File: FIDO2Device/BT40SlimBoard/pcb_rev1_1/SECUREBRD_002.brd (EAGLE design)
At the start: 30 x 30 mm, 31 parts, among them CN1 2137160001, CN2 IF_5PIN_H, CN3 IF_2PIN_SOL, SW1 SKRPACE010, SW2 SKRPACE010, SW3 SKTADAE010, U1 BT40, U2 ADP122ACPZ-3.3-R7

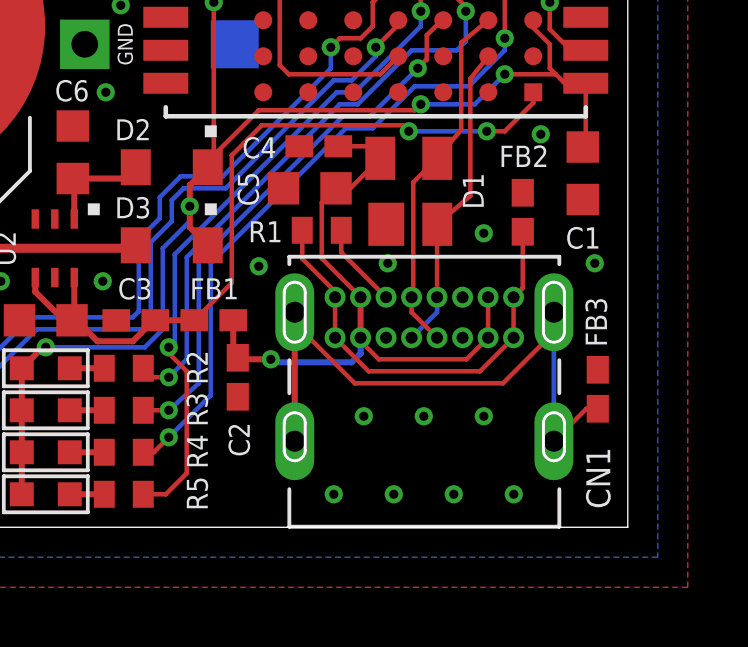
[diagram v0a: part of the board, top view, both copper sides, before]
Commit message: 回路図を更新
・USB-Cプラグ部品を`USB4105-GF-A`に更新
（前回試作失敗の原因となった部品`2137160001`から差し替え）
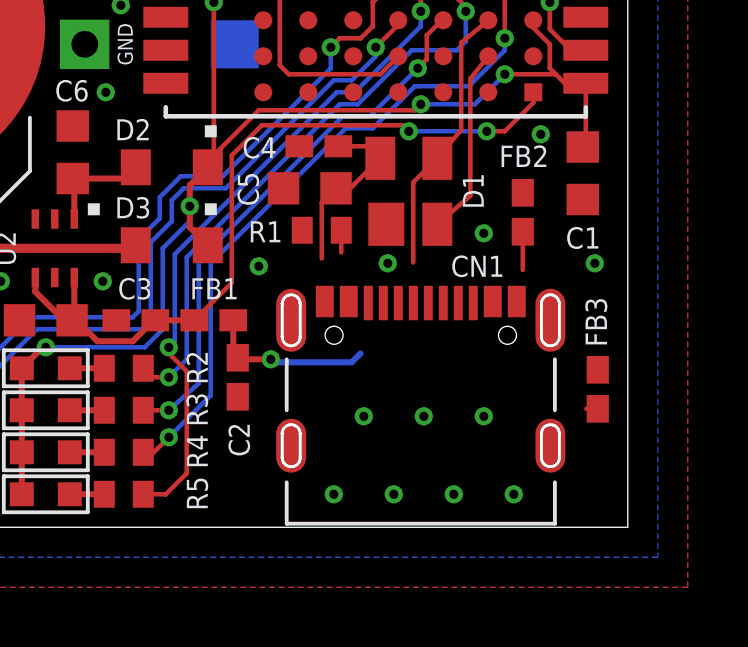
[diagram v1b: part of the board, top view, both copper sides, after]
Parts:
- CN1: value 2137160001 -> USB4105-GF-A; device Connectors:2137160001 -> Connectors:USB4105-GF-A
- moved CN1 0.29 mm to (23.1, 6.90)
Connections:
- net USB_GND: no longer CN1.A12, CN1.B12
- net VBUS: no longer CN1.A9, CN1.B9
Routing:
- net FG: track 21.7 -> 0.38 mm
- net USB_GND: track 14.6 -> 1.27 mm
- net VBUS: track 21.7 -> 11.6 mm
- net D_N: track 10.5 -> 6.32 mm
- net D_P: track 12.0 -> 9.12 mm
- net N$2: track 2.85 -> 0.74 mm
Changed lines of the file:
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@@
 <attribute name="VALUE" x="6.29" y="6.87" size="0.7" layer="27" rot="R270"/>
-</element>
-<element name="CN1" library="Connectors" package="2137160001" value="2137160001" x="23.2178" y="7.1688" smashed="yes">
-<attribute name="NAME" x="28.6178" y="2.6688" size="0.8" layer="25" rot="R270"/>
-<attribute name="VALUE" x="23.5178" y="9.3688" size="0.8" layer="27"/>
 </element>
 <element name="R1" library="Parts" package="R0402" value="5.1k" x="19.8" y="9.9" smashed="yes">
@@
 </element>
 <element name="CN3" library="Connectors" package="SOLPAD_2PIN" value="IF_2PIN_SOL" x="16.9" y="16.1" rot="MR90"/>
+<element name="CN1" library="Connectors" package="USB4105-GF-A" value="USB4105-GF-A" x="23.1" y="6.9" smashed="yes">
+<attribute name="NAME" x="24.1" y="8.35" size="0.7" layer="25"/>
+<attribute name="VALUE" x="23.4" y="8.5" size="0.8" layer="27"/>
+</element>
 </elements>
 <signals>
@@
 <contactref element="C5" pad="1"/>
 <contactref element="D1" pad="4"/>
-<contactref element="CN1" pad="A4"/>
-<contactref element="CN1" pad="B9"/>
-<contactref element="CN1" pad="A9"/>
-<contactref element="CN1" pad="B4"/>
-<wire x1="25.3428" y1="6.3188" x2="25.3428" y2="7.6688" width="0.1524" layer="1"/>
-<wire x1="21.0928" y1="7.6688" x2="21.0928" y2="6.3188" width="0.2032" layer="1"/>
-<wire x1="21.0928" y1="6.3188" x2="21.0928" y2="6.2072" width="0.1524" layer="1"/>
-<wire x1="21.0928" y1="6.2072" x2="21.7" y2="5.6" width="0.1524" layer="1"/>
-<wire x1="25.3428" y1="6.3188" x2="24.624" y2="5.6" width="0.1524" layer="1"/>
-<wire x1="24.624" y1="5.6" x2="21.7" y2="5.6" width="0.1524" layer="1"/>
-<wire x1="21.0928" y1="7.6688" x2="19.8" y2="8.9616" width="0.1524" layer="1"/>
 <wire x1="19.8" y1="8.9616" x2="19.8" y2="10.825" width="0.1524" layer="1"/>
 <wire x1="20.275" y1="11.3" x2="19.8" y2="10.825" width="0.1524" layer="1"/>
 <via x="18.1" y="5.6" extent="1-16" drill="0.3048"/>
-<wire x1="21.0928" y1="6.2072" x2="21.0928" y2="6.3188" width="0.1524" layer="16"/>
 <wire x1="16.85" y1="6.9" x2="16.85" y2="5.8" width="0.2032" layer="1"/>
 <wire x1="16.85" y1="5.8" x2="17" y2="5.65" width="0.2032" layer="1"/>
@@
 <wire x1="18.2" y1="5.5" x2="20.8" y2="5.5" width="0.2032" layer="16"/>
 <wire x1="20.8" y1="5.5" x2="21.0928" y2="5.7928" width="0.2032" layer="16"/>
-<wire x1="21.0928" y1="6.3188" x2="21.0928" y2="5.7928" width="0.2032" layer="16"/>
 <wire x1="20.275" y1="11.3" x2="20.75" y2="11.3" width="0.1524" layer="1"/>
 <wire x1="20.75" y1="11.3" x2="21.75" y2="12.3" width="0.1524" layer="1"/>
@@
 <wire x1="17.05" y1="5.6" x2="18.1" y2="5.6" width="0.2032" layer="1"/>
 <wire x1="18.2" y1="5.5" x2="18.1" y2="5.6" width="0.2032" layer="16"/>
+<contactref element="CN1" pad="A4"/>
+<contactref element="CN1" pad="B4"/>
+<wire x1="21.0928" y1="5.7928" x2="25.5" y2="7.525" width="0" layer="19" extent="1-16"/>
+<wire x1="20.7" y1="7.525" x2="21.0928" y2="5.7928" width="0" layer="19" extent="1-16"/>
+<wire x1="19.8" y1="8.9616" x2="20.7" y2="7.525" width="0" layer="19" extent="1-1"/>
 </signal>
 <signal name="USB_GND">
 <contactref element="FB2" pad="1"/>
-<contactref element="R1" pad="1"/>
-<contactref element="CN1" pad="A12"/>
+<wire x1="26.5" y1="9.85" x2="26.5" y2="8.576" width="0.1524" layer="1"/>
 <contactref element="CN1" pad="B1"/>
 <contactref element="CN1" pad="A1"/>
-<contactref element="CN1" pad="B12"/>
-<wire x1="26.5" y1="9.85" x2="26.5" y2="7.976" width="0.1524" layer="1"/>
-<wire x1="26.5" y1="7.976" x2="26.1928" y2="7.6688" width="0.1524" layer="1"/>
-<wire x1="20.2428" y1="6.3188" x2="20.2428" y2="7.6688" width="0.1524" layer="1"/>
-<wire x1="26.1928" y1="6.3188" x2="25.074" y2="5.2" width="0.1524" layer="1"/>
-<wire x1="20.2428" y1="6.3188" x2="21.3616" y2="5.2" width="0.1524" layer="1"/>
-<wire x1="26.1928" y1="6.3188" x2="26.1928" y2="7.6688" width="0.1524" layer="1"/>
-<wire x1="25.074" y1="5.2" x2="21.3616" y2="5.2" width="0.1524" layer="1"/>
-<wire x1="20.2428" y1="7.6688" x2="20.2428" y2="7.8572" width="0.1524" layer="1"/>
-<wire x1="20.2428" y1="7.8572" x2="19.15" y2="8.95" width="0.1524" layer="1"/>
-<wire x1="19.15" y1="9.9" x2="19.15" y2="8.95" width="0.1524" layer="1"/>
+<contactref element="R1" pad="1"/>
+<wire x1="26.3" y1="7.525" x2="26.5" y2="8.576" width="0" layer="19" extent="1-1"/>
+<wire x1="19.9" y1="7.525" x2="26.3" y2="7.525" width="0" layer="19" extent="1-1"/>
+<wire x1="19.15" y1="9.9" x2="19.9" y2="7.525" width="0" layer="19" extent="1-1"/>
 </signal>
 <signal name="FG">
 <contactref element="FB3" pad="1"/>
+<wire x1="29" y1="3.95" x2="28.619" y2="3.95" width="0.1524" layer="1"/>
 <contactref element="CN1" pad="FG4"/>
+<contactref element="CN1" pad="FG3"/>
 <contactref element="CN1" pad="FG1"/>
 <contactref element="CN1" pad="FG2"/>
-<contactref element="CN1" pad="FG3"/>
-<wire x1="27.5378" y1="2.8688" x2="27.5378" y2="7.1688" width="0.1524" layer="16"/>
-<wire x1="18.8978" y1="7.1688" x2="18.8978" y2="6.8022" width="0.1524" layer="1"/>
-<wire x1="18.8978" y1="6.8022" x2="20.9" y2="4.8" width="0.1524" layer="1"/>
-<wire x1="25.8378" y1="4.8" x2="27.5378" y2="6.5" width="0.1524" layer="1"/>
-<wire x1="27.5378" y1="6.5" x2="27.5378" y2="7.1688" width="0.1524" layer="1"/>
-<wire x1="29" y1="3.95" x2="28.619" y2="3.95" width="0.1524" layer="1"/>
-<wire x1="28.619" y1="3.95" x2="27.5378" y2="2.8688" width="0.1524" layer="1"/>
-<wire x1="25.8378" y1="4.8" x2="20.9" y2="4.8" width="0.1524" layer="1"/>
-<wire x1="18.8978" y1="2.8688" x2="18.8978" y2="7.1688" width="0.2032" layer="1"/>
+<wire x1="27.42" y1="2.72" x2="28.619" y2="3.95" width="0" layer="19" extent="1-1"/>
+<wire x1="27.42" y1="6.9" x2="28.619" y2="3.95" width="0" layer="19" extent="1-1"/>
+<wire x1="18.78" y1="6.9" x2="27.42" y2="6.9" width="0" layer="19" extent="1-1"/>
+<wire x1="18.78" y1="2.72" x2="18.78" y2="6.9" width="0" layer="19" extent="1-1"/>
 </signal>
 <signal name="D_N">
 <contactref element="D1" pad="2"/>
 <contactref element="U1" pad="E5"/>
-<contactref element="CN1" pad="A7"/>
-<contactref element="CN1" pad="B7"/>
 <wire x1="25.35" y1="15.7" x2="24.7524" y2="14.95" width="0.1524" layer="1"/>
 <wire x1="23.65" y1="10.1" x2="24.7524" y2="11.05" width="0.1524" layer="1"/>
 <wire x1="24.7524" y1="11.05" x2="24.7524" y2="14.95" width="0.1524" layer="1"/>
 <wire x1="23.65" y1="10.1" x2="23.6428" y2="10.0928" width="0.1524" layer="1"/>
-<wire x1="23.6428" y1="10.0928" x2="23.6428" y2="7.6688" width="0.1524" layer="1"/>
-<wire x1="22.7928" y1="6.3188" x2="23.6428" y2="7.1688" width="0.1524" layer="16"/>
-<wire x1="23.6428" y1="7.1688" x2="23.6428" y2="7.6688" width="0.1524" layer="16"/>
+<contactref element="CN1" pad="A7"/>
+<contactref element="CN1" pad="B7"/>
+<wire x1="23.35" y1="7.475" x2="23.6428" y2="10.0928" width="0" layer="19" extent="1-1"/>
+<wire x1="22.35" y1="7.475" x2="23.35" y2="7.475" width="0" layer="19" extent="1-1"/>
 </signal>
 <signal name="D_P">
 <contactref element="D1" pad="3"/>
 <contactref element="U1" pad="E4"/>
-<contactref element="CN1" pad="A6"/>
-<contactref element="CN1" pad="B6"/>
 <wire x1="25.35" y1="16.9" x2="24.4476" y2="16.15" width="0.1524" layer="1"/>
 <wire x1="24.4476" y1="16.15" x2="24.4476" y2="13.25" width="0.1524" layer="1"/>
 <wire x1="23.65" y1="12.3" x2="24.4476" y2="13.25" width="0.1524" layer="1"/>
 <wire x1="23.65" y1="12.3" x2="22.85" y2="11.5" width="0.1524" layer="1"/>
-<wire x1="22.85" y1="11.5" x2="22.85" y2="7.726" width="0.1524" layer="1"/>
-<wire x1="22.7928" y1="7.6688" x2="22.85" y2="7.726" width="0.1524" layer="1"/>
-<wire x1="22.7928" y1="7.6688" x2="22.7928" y2="7.1688" width="0.1524" layer="1"/>
-<wire x1="22.7928" y1="7.1688" x2="23.6428" y2="6.3188" width="0.1524" layer="1"/>
+<wire x1="22.85" y1="11.5" x2="22.85" y2="8.826" width="0.1524" layer="1"/>
+<contactref element="CN1" pad="A6"/>
+<contactref element="CN1" pad="B6"/>
+<wire x1="22.85" y1="7.475" x2="22.85" y2="8.826" width="0" layer="19" extent="1-1"/>
+<wire x1="23.85" y1="7.475" x2="22.85" y2="7.475" width="0" layer="19" extent="1-1"/>
 </signal>
 <signal name="LED2">
@@
 </signal>
 <signal name="N$2">
+<contactref element="R1" pad="2"/>
+<wire x1="20.45" y1="9.1616" x2="20.45" y2="9.9" width="0.1524" layer="1"/>
 <contactref element="CN1" pad="A5"/>
-<contactref element="R1" pad="2"/>
-<wire x1="21.9428" y1="7.6688" x2="20.45" y2="9.1616" width="0.1524" layer="1"/>
-<wire x1="20.45" y1="9.1616" x2="20.45" y2="9.9" width="0.1524" layer="1"/>
+<wire x1="21.85" y1="7.475" x2="20.45" y2="9.1616" width="0" layer="19" extent="1-1"/>
 </signal>
 <signal name="N$3">
